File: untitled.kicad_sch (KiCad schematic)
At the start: 8 parts, among them J1 Conn_01x18_MountingPin, J2 Conn_01x04, J3 Conn_02x25_Odd_Even, J4 Conn_02x25_Odd_Even, U1 STM32F407ZGTx

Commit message: 测试
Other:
- note added: "1"
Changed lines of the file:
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@@
+		)
+	)
+	(text "1"
+		(exclude_from_sim no)
+		(at 62.23 177.8 0)
+		(effects
+			(font
+				(size 1.27 1.27)
+			)
 		)
 	)

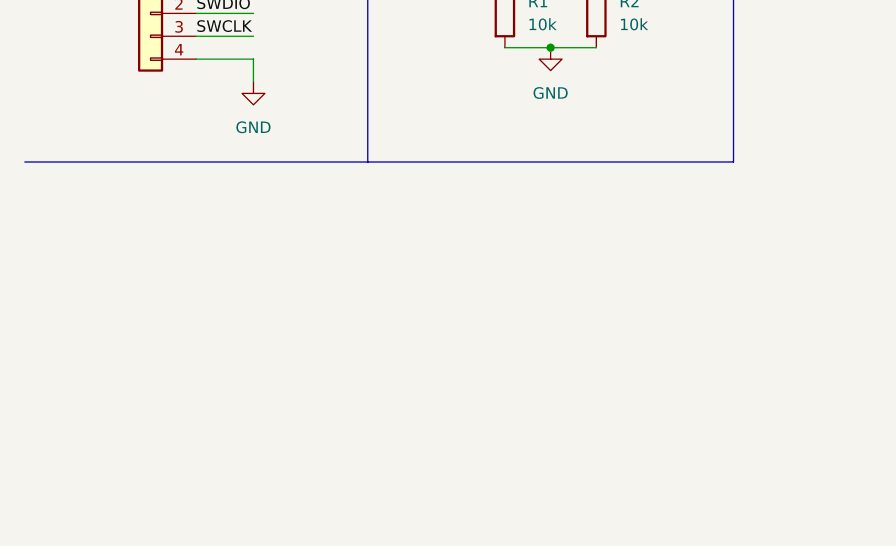
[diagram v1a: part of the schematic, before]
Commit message: 完成去耦电容部分
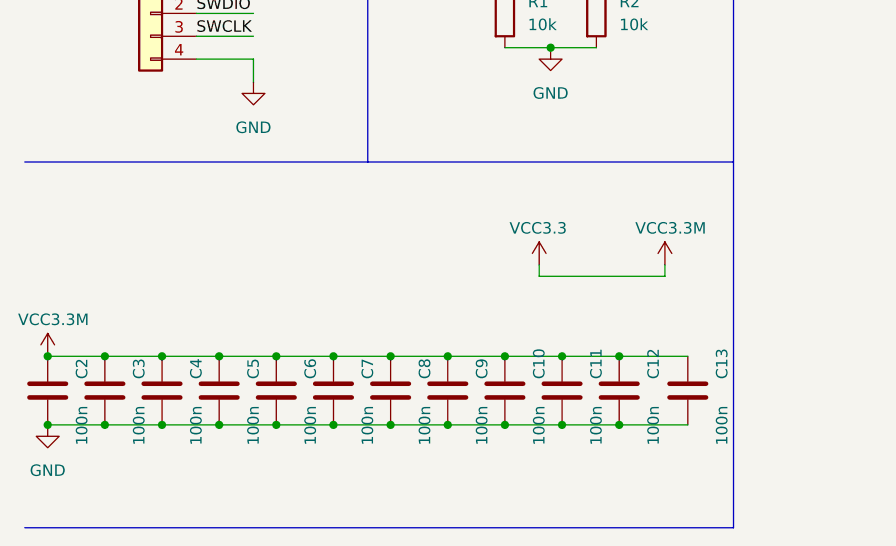
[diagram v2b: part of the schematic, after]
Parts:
- added C10, C11, C12, C13, C2, C3, C4, C5, C6, C7, C8, C9: 100n, symbol Device:C
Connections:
- net GND: now also C10.2, C11.2, C12.2, C13.2, C2.2, C3.2, C4.2, C5.2, C6.2, C7.2, C8.2, C9.2
- net VCC3.3: now also C10.1, C11.1, C12.1, C13.1, C2.1, C3.1, C4.1, C5.1, C6.1, C7.1, C8.1, C9.1

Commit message: 补丁
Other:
- note removed: "1"
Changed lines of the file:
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@@
-		)
-	)
-	(text "1"
-		(exclude_from_sim no)
-		(at 62.23 177.8 0)
-		(effects
-			(font
-				(size 1.27 1.27)
-			)
 		)
 	)
